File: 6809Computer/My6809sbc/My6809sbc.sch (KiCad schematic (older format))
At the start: 55 parts, among them J1 HEADER 2x5, J10 Conn_01x04, J11 AUDIO OUT, J12 HEADER 2x20, J13 Conn_01x02, J2 HEADER 1x6, J3 HEADER 2x5, J4 HEADER 2x5, J5 TP1, J6 TP2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

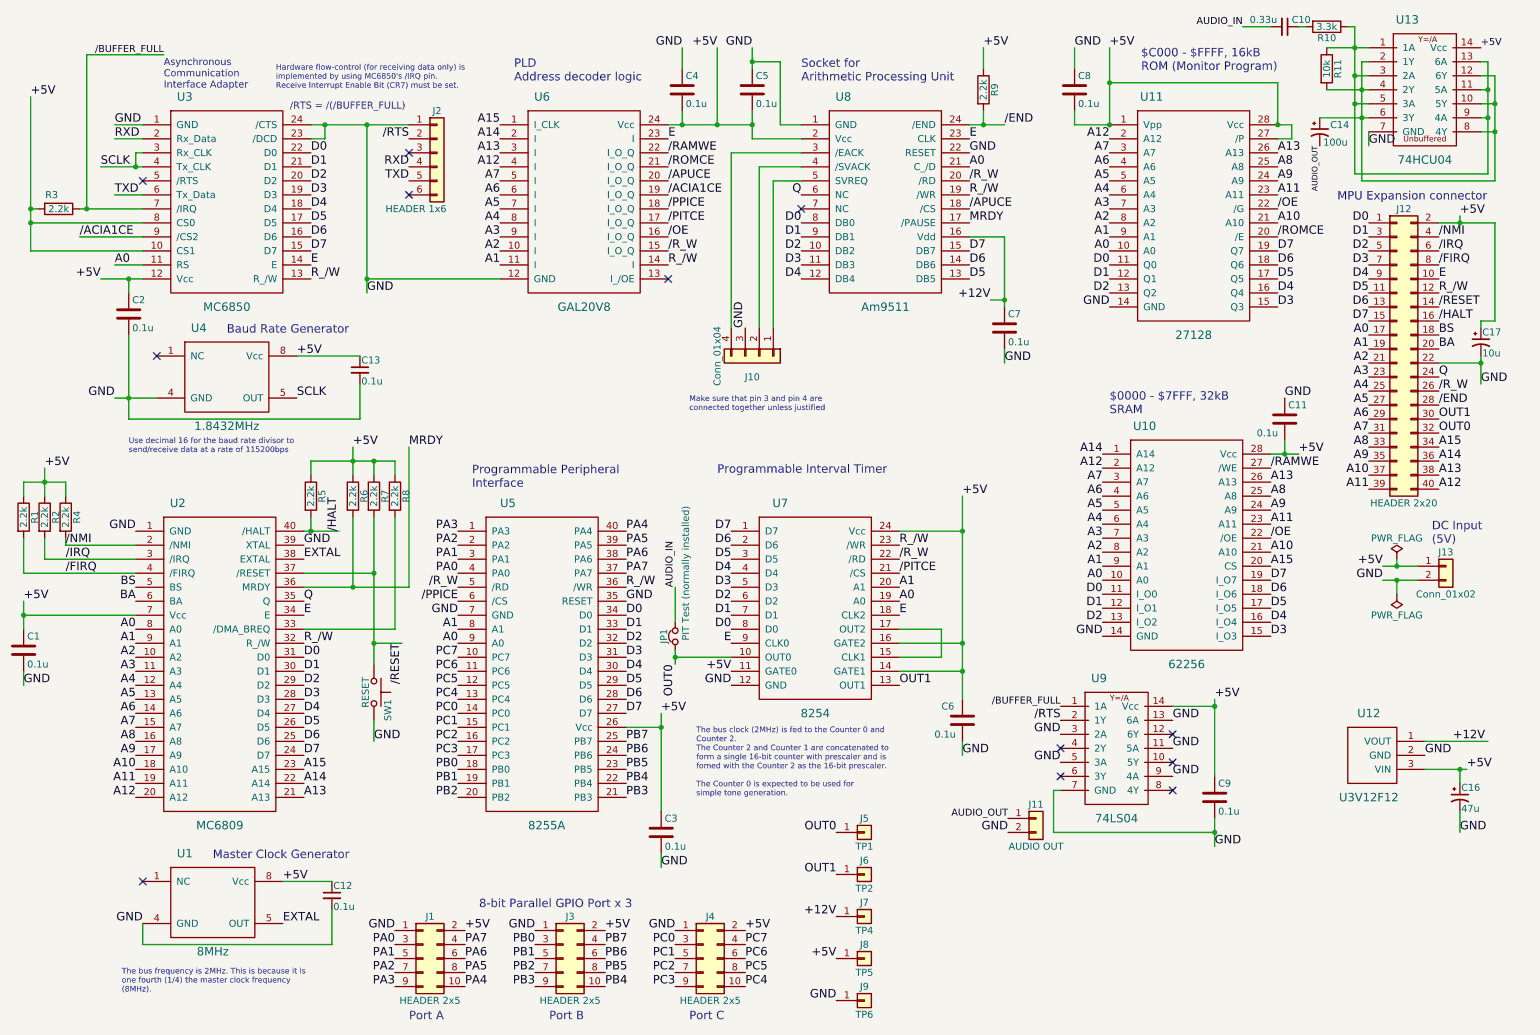
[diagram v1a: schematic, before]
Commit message: Update design materials of 6809sbc and old files are moved to the archive directory (REV2). Now My6809sbc directory contains REV3 design materials.
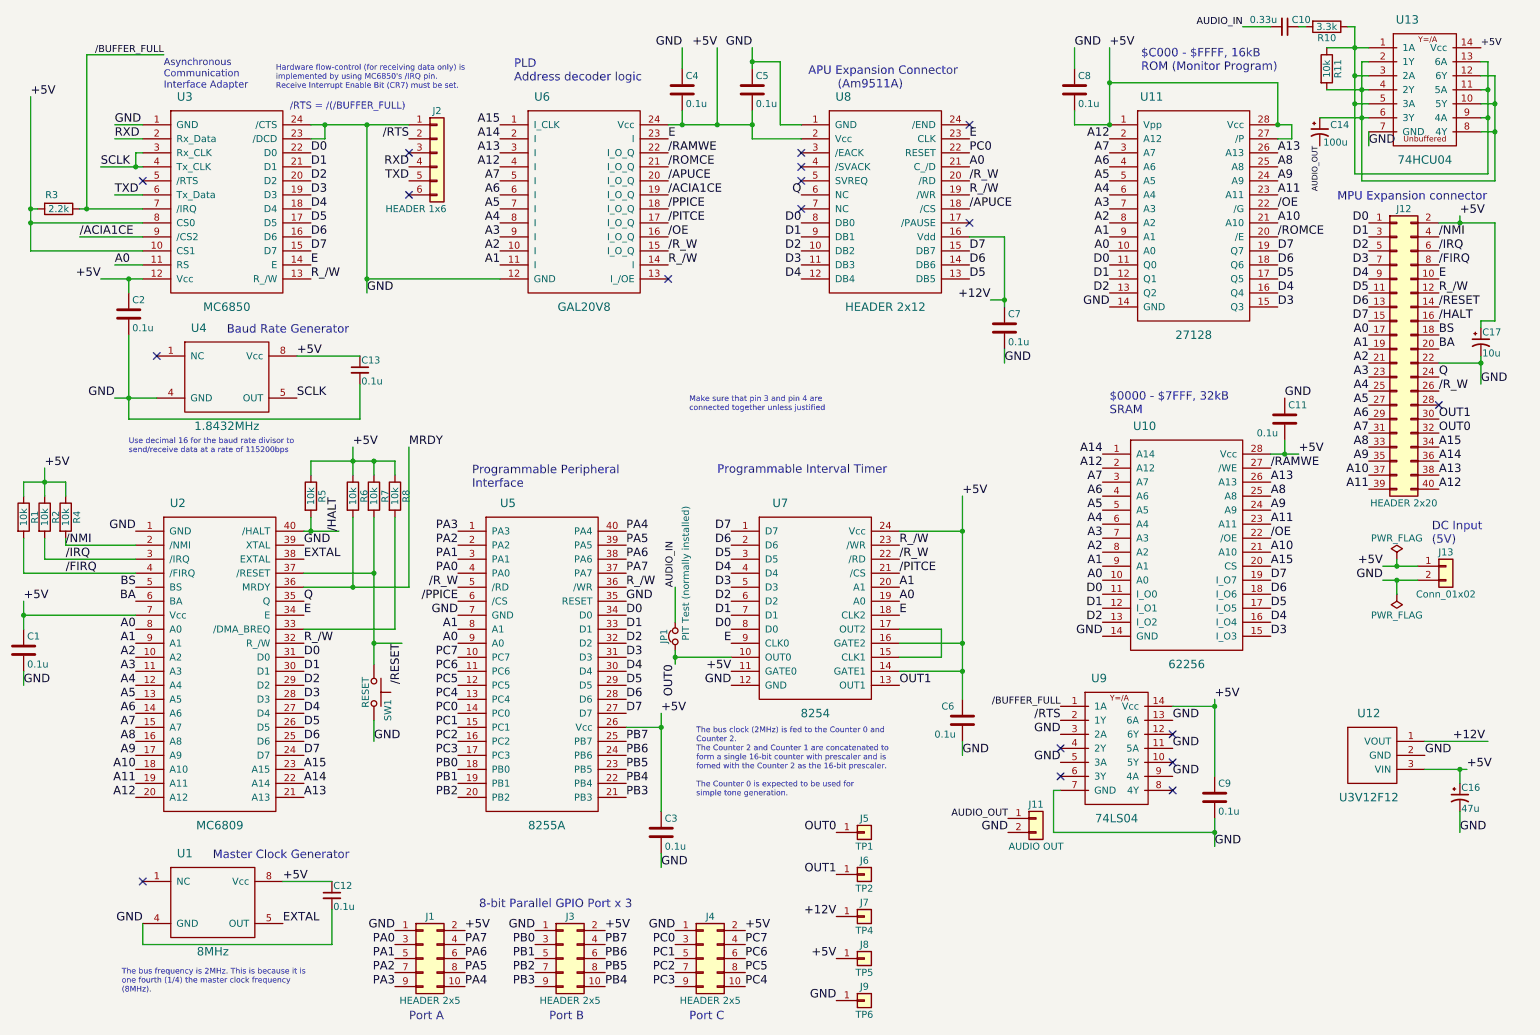
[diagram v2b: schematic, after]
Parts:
- removed J10: Conn_01x04, Pin_Headers:Pin_Header_Straight_1x04_Pitch2.54mm, symbol Conn_01x04
- removed R9: 2.2k, Resistors_THT:R_Axial_DIN0207_L6.3mm_D2.5mm_P10.16mm_Horizontal, symbol R
- R1, R2, R4, R5, R6, R7, R8: value 2.2k -> 10k
- U8: value Am9511 -> HEADER 2x12
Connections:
- net GND: no longer U8.22 (RESET)
- net MRDY: no longer U8.17 (/PAUSE)
- net PC0: now also U8.22 (RESET)
- net /END: no longer names the net of U8.24 (/END)
- net /END: no longer J12.28 (Pin_28)
- no-connect marks 12 -> 18
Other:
- note added: "APU Expansion Connector\n (Am9511A)"
- note removed: "Socket for\nArithmetic Processing Unit"
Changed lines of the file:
@@
 Sheet 1 1
 Title "MUTIF09 6809 Single Board Computer"
-Date "2018-09-10"
-Rev "2"
+Date "2018-10-12"
+Rev "3"
 Comp "MUTIF09 Project"
 Comment1 ""
@@
 P 6800 1850
 F 0 "U8" H 6500 2600 60  0000 C CNN
-F 1 "Am9511" H 6800 1100 60  0000 C CNN
+F 1 "HEADER 2x12" H 6800 1100 60  0000 C CNN
 F 2 "Housings_DIP:DIP-24_W15.24mm_Socket" H 6800 1400 60  0001 C CNN
 F 3 "" H 6800 1400 60  0001 C CNN
@@
 Text Label 7400 1400 0    60   ~ 0
 E
-Text Label 7400 1500 0    60   ~ 0
-GND
 Text Label 7400 1600 0    60   ~ 0
 A0
@@
 P 650 4100
 F 0 "R1" V 730 4100 50  0000 C CNN
-F 1 "2.2k" V 650 4100 50  0000 C CNN
+F 1 "10k" V 650 4100 50  0000 C CNN
 F 2 "Resistors_THT:R_Axial_DIN0207_L6.3mm_D2.5mm_P10.16mm_Horizontal" V 580 4100 50  0001 C CNN
 F 3 "" H 650 4100 50  0001 C CNN
@@
 P 800 4100
 F 0 "R2" V 880 4100 50  0000 C CNN
-F 1 "2.2k" V 800 4100 50  0000 C CNN
+F 1 "10k" V 800 4100 50  0000 C CNN
 F 2 "Resistors_THT:R_Axial_DIN0207_L6.3mm_D2.5mm_P10.16mm_Horizontal" V 730 4100 50  0001 C CNN
 F 3 "" H 800 4100 50  0001 C CNN
@@
 P 950 4100
 F 0 "R4" V 1030 4100 50  0000 C CNN
-F 1 "2.2k" V 950 4100 50  0000 C CNN
+F 1 "10k" V 950 4100 50  0000 C CNN
 F 2 "Resistors_THT:R_Axial_DIN0207_L6.3mm_D2.5mm_P10.16mm_Horizontal" V 880 4100 50  0001 C CNN
 F 3 "" H 950 4100 50  0001 C CNN
@@
 P 2700 3950
 F 0 "R5" V 2780 3950 50  0000 C CNN
-F 1 "2.2k" V 2700 3950 50  0000 C CNN
+F 1 "10k" V 2700 3950 50  0000 C CNN
 F 2 "Resistors_THT:R_Axial_DIN0207_L6.3mm_D2.5mm_P10.16mm_Horizontal" V 2630 3950 50  0001 C CNN
 F 3 "" H 2700 3950 50  0001 C CNN
@@
 P 3000 3950
 F 0 "R6" V 3080 3950 50  0000 C CNN
-F 1 "2.2k" V 3000 3950 50  0000 C CNN
+F 1 "10k" V 3000 3950 50  0000 C CNN
 F 2 "Resistors_THT:R_Axial_DIN0207_L6.3mm_D2.5mm_P10.16mm_Horizontal" V 2930 3950 50  0001 C CNN
 F 3 "" H 3000 3950 50  0001 C CNN
@@
 P 3150 3950
 F 0 "R7" V 3230 3950 50  0000 C CNN
-F 1 "2.2k" V 3150 3950 50  0000 C CNN
+F 1 "10k" V 3150 3950 50  0000 C CNN
 F 2 "Resistors_THT:R_Axial_DIN0207_L6.3mm_D2.5mm_P10.16mm_Horizontal" V 3080 3950 50  0001 C CNN
 F 3 "" H 3150 3950 50  0001 C CNN
@@
 P 3300 3950
 F 0 "R8" V 3380 3950 50  0000 C CNN
-F 1 "2.2k" V 3300 3950 50  0000 C CNN
+F 1 "10k" V 3300 3950 50  0000 C CNN
 F 2 "Resistors_THT:R_Axial_DIN0207_L6.3mm_D2.5mm_P10.16mm_Horizontal" V 3230 3950 50  0001 C CNN
 F 3 "" H 3300 3950 50  0001 C CNN
@@
 Text Notes 3850 3900 0    60   ~ 0
 Programmable Peripheral\nInterface
-$Comp
-L R R9
-U 1 1 5B2DC0AA
-P 7500 1050
-F 0 "R9" V 7580 1050 50  0000 C CNN
-F 1 "2.2k" V 7500 1050 50  0000 C CNN
-F 2 "Resistors_THT:R_Axial_DIN0207_L6.3mm_D2.5mm_P10.16mm_Horizontal" V 7430 1050 50  0001 C CNN
-F 3 "" H 7500 1050 50  0001 C CNN
-	1    7500 1050
-	1    0    0    -1
-$EndComp
-Text Label 7500 750  0    60   ~ 0
-+5V
-Text Label 7650 1300 0    60   ~ 0
-/END
-Text Label 10750 3300 0    60   ~ 0
-/END
-Text Notes 6200 1000 0    60   ~ 0
-         Socket for\nArithmetic Processing Unit
+Text Notes 6250 1050 0    60   ~ 0
+APU Expansion Connector\n        (Am9511A)
 NoConn ~ 8050 5950
 Text Notes 4150 1000 0    60   ~ 0
@@
 Text Label 3400 3600 0    60   ~ 0
 MRDY
-Text Label 7400 2000 0    60   ~ 0
-MRDY
 Text Label 10750 3100 0    60   ~ 0
 Q
@@
 Wire Wire Line
 	7200 5100 6900 5100
-Wire Wire Line
-	7500 750  7500 900
-Wire Wire Line
-	7400 1300 7650 1300
-Wire Wire Line
-	7500 1200 7500 1300
-Connection ~ 7500 1300
 Connection ~ 700  2000
 Wire Wire Line
@@
 Connection ~ 10900 5900
 Wire Wire Line
-	5900 1600 6200 1600
-Wire Wire Line
-	6000 1700 6200 1700
-Wire Wire Line
 	6050 1300 6050 850
-Wire Wire Line
-	6200 1500 5700 1500
-Wire Wire Line
-	5700 1500 5700 2750
-Wire Wire Line
-	5900 2750 5900 1600
-Wire Wire Line
-	6000 2750 6000 1700
-Text Label 5800 2750 1    60   ~ 0
-GND
 Text Notes 5400 3350 0    40   ~ 0
 Make sure that pin 3 and pin 4 are \nconnected together unless justified
 Text Label 6200 1800 2    60   ~ 0
 Q
-$Comp
-L Conn_01x04 J10
-U 1 1 5B99B0DD
-P 5900 2950
-F 0 "J10" V 6050 2900 50  0000 C CNN
-F 1 "Conn_01x04" H 5900 2650 50  0000 C CNN
-F 2 "Pin_Headers:Pin_Header_Straight_1x04_Pitch2.54mm" H 5900 2950 50  0001 C CNN
-F 3 "" H 5900 2950 50  0001 C CNN
-	1    5900 2950
-	0    1    1    0
-$EndComp
+Text Label 7400 1500 0    60   ~ 0
+PC0
+NoConn ~ 6200 1500
+NoConn ~ 6200 1600
+NoConn ~ 6200 1700
+NoConn ~ 7400 2000
+NoConn ~ 7400 1300
+NoConn ~ 10750 3300
 $EndSCHEMATC
